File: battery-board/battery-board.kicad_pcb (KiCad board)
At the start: 4 copper layers, 50.1 x 70.1 mm, 34 parts, among them P1 CONN_01X14, P2 CONN_01X14, P3 CONN_01X02, P4 CONN_01X01, SW1 SW_PUSH, U1 BMP180, U2 MAX1724, U3 SI7021

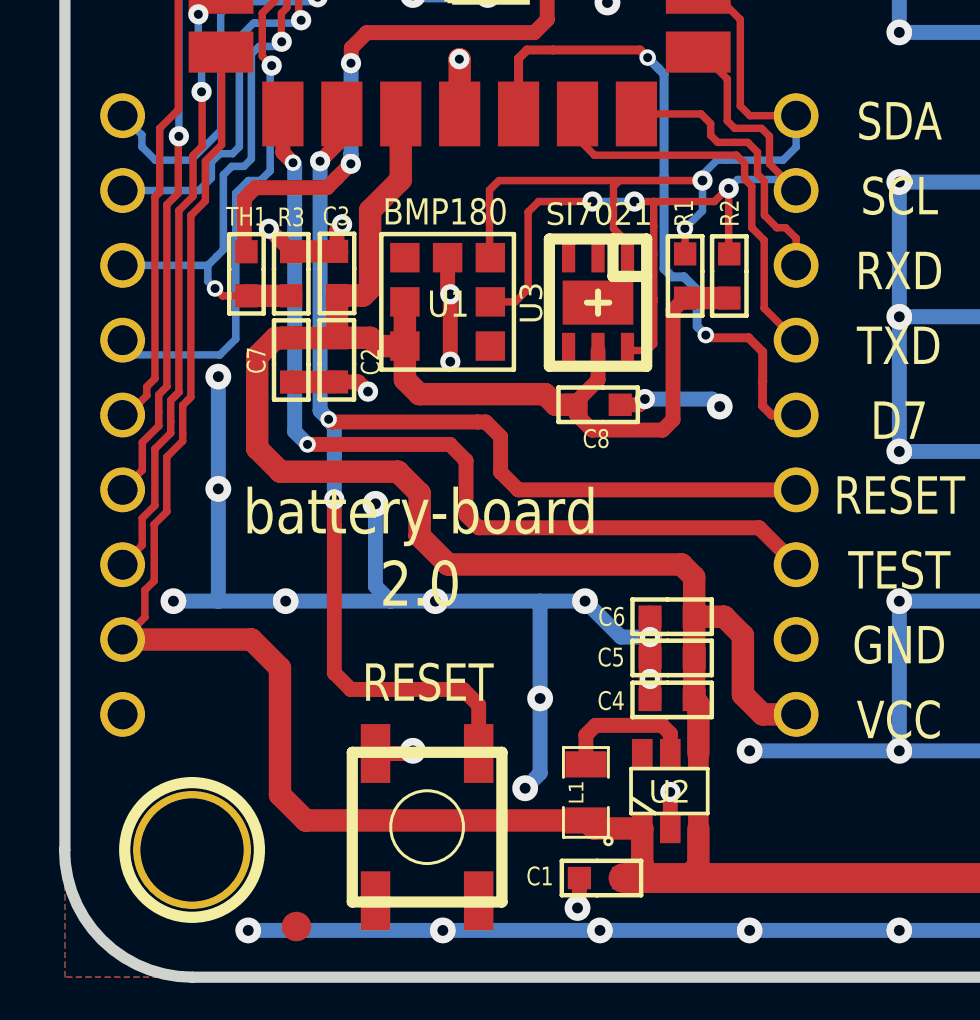
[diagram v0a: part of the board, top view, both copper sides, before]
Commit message: New light sensor
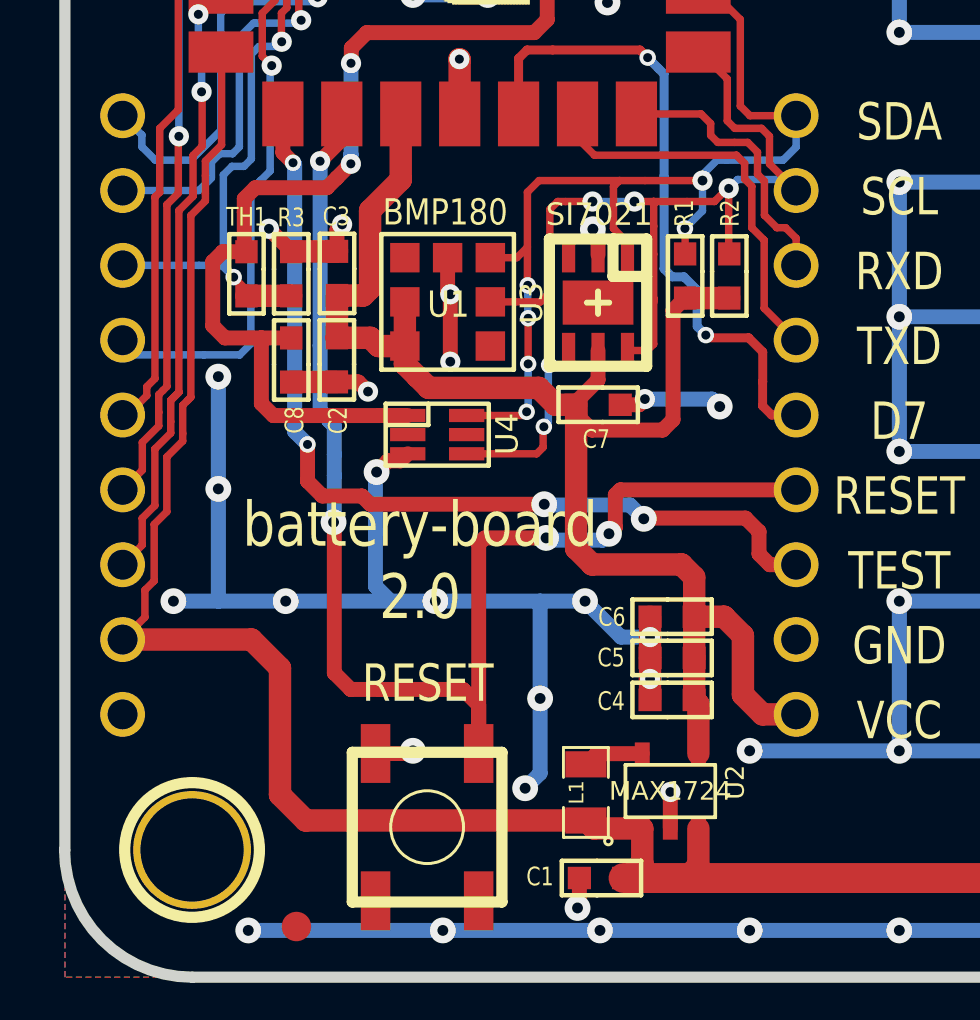
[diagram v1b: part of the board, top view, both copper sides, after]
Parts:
- added U4: TSL2561, mysmd:uDFN-6, F.Cu at (97.1, 85.8)
- U2: footprint libcms:SOT23_6 -> libcms:SOT23-5
- renumbered C8 to C7, C7 to C8
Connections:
- C8 pad 1: VCC -> /D22
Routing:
- net VCC: track 67.8 -> 53.2 mm
- net /D22: track 36.0 -> 49.7 mm
- net /I2C_SCL: track 29.0 -> 37.2 mm, vias 3 -> 5
- net /I2C_SDA: track 27.2 -> 34.6 mm, vias 2 -> 6
- net GND: track 517.2 -> 520.5 mm, vias 149 -> 150
- net Net-(L1-Pad2): track 4.79 -> 2.06 mm
- net /RESET: track 44.5 -> 46.3 mm, vias 3 -> 4
- net /TEST: track 31.7 -> 31.8 mm, vias 2 -> 4

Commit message: Solder mask clearance fixed
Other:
- rule pad_to_mask_clearance: 0 -> 0.0762
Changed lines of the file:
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@@
-(kicad_pcb (version 4) (host pcbnew 0.201601141852+6469~42~ubuntu14.04.1-product)
+(kicad_pcb (version 4) (host pcbnew 0.201601211448+6504~42~ubuntu14.04.1-product)
   (general
     (links 91)
@@
     (pad_size 1.524 1.524)
     (pad_drill 1.016)
-    (pad_to_mask_clearance 0)
+    (pad_to_mask_clearance 0.0762)
+    (solder_mask_min_width 0.1016)
     (aux_axis_origin 162.52952 122.1486)
     (visible_elements FFFFF7BF)
